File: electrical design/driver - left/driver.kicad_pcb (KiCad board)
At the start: 2 copper layers, 69 x 34 mm, 40 parts, among them J1 Conn_01x02_Female, J2 Conn_01x11_Male, M1C3 1µf, M1C8 33nF, M1CP1 680µF, M1D1 RED, M1D2 GREEN, M1J1 Conn_01x06_Female, M1Q1 MOSFET-NCH-FDD8780, M1R0 4.7k, M1R10 1k, M1R4 1k, M1R5 3.24k, M1R6 10k, M1R71 1k, M1R72 10k, M1R81 10k, M1R82 1k, M1R9 3.24k, M1U1 VNH5019A-E, M2C3 1µf, M2C8 33nF, M2CP1 680µF, M2D1 RED, M2D2 GREEN, M2J1 Conn_01x06_Female, M2Q1 MOSFET-NCH-FDD8780, M2R0 4.7k, M2R10 1k, M2R4 1k, M2R5 3.24k, M2R6 10k, M2R71 1k, M2R72 10k, M2R81 10k, M2R82 1k, M2R9 3.24k, M2U1 VNH5019A-E, U1 74LVC2G07GW,125

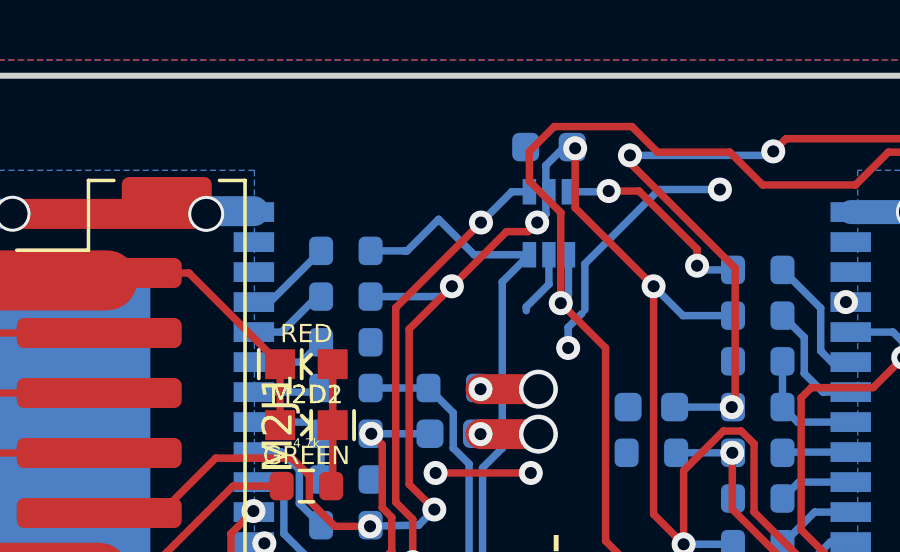
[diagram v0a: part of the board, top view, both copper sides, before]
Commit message: rename some files
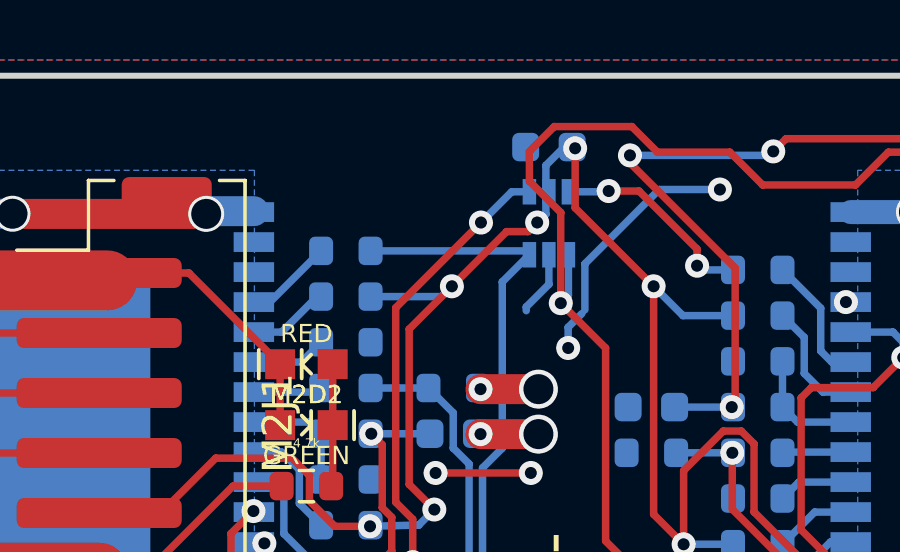
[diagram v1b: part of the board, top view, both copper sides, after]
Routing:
- net /M2INA: track 41.2 -> 40.3 mm
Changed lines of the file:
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@@
   (segment (start 142.155502 97.581698) (end 143.504898 97.581698) (width 1) (layer "B.Cu") (net 26))
   (segment (start 139.3758 100.3614) (end 142.155502 97.581698) (width 1) (layer "B.Cu") (net 26))
+  (segment (start 155.4408 98.819235) (end 160.604635 98.819235) (width 0.25) (layer "B.Cu") (net 27))
   (segment (start 159.172889 106.053911) (end 159.830111 105.396689) (width 0.25) (layer "B.Cu") (net 27))
-  (segment (start 156.658165 98.819235) (end 157.7104 97.767) (width 0.25) (layer "B.Cu") (net 27))
   (segment (start 159.172889 120.996689) (end 159.172889 106.053911) (width 0.25) (layer "B.Cu") (net 27))
-  (segment (start 155.4408 98.819235) (end 156.580635 98.819235) (width 0.25) (layer "B.Cu") (net 27))
+  (segment (start 160.604635 98.819235) (end 160.7354 98.95) (width 0.25) (layer "B.Cu") (net 27))
   (segment (start 159.830111 99.855289) (end 160.7354 98.95) (width 0.25) (layer "B.Cu") (net 27))
   (segment (start 159.830111 105.396689) (end 159.830111 99.855289) (width 0.25) (layer "B.Cu") (net 27))
-  (segment (start 156.580635 98.819235) (end 156.658165 98.819235) (width 0.25) (layer "B.Cu") (net 27))
   (segment (start 160.312711 122.136511) (end 159.172889 120.996689) (width 0.25) (layer "B.Cu") (net 27))
   (segment (start 170.1102 124.2) (end 168.046711 122.136511) (width 0.25) (layer "B.Cu") (net 27))
-  (segment (start 158.8934 98.95) (end 160.7354 98.95) (width 0.25) (layer "B.Cu") (net 27))
   (segment (start 168.046711 122.136511) (end 160.312711 122.136511) (width 0.25) (layer "B.Cu") (net 27))
-  (segment (start 157.7104 97.767) (end 158.8934 98.95) (width 0.25) (layer "B.Cu") (net 27))
   (segment (start 152.083635 100.5264) (end 153.7908 98.819235) (width 0.25) (layer "B.Cu") (net 28))
   (segment (start 151.5508 100.5264) (end 152.083635 100.5264) (width 0.25) (layer "B.Cu") (net 28))
